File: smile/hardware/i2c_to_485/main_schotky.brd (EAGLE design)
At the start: 34.3 x 45.2 mm, 12 parts, among them IC1 MAX481CSA, IC2 MAX481CSA, U1 7402D

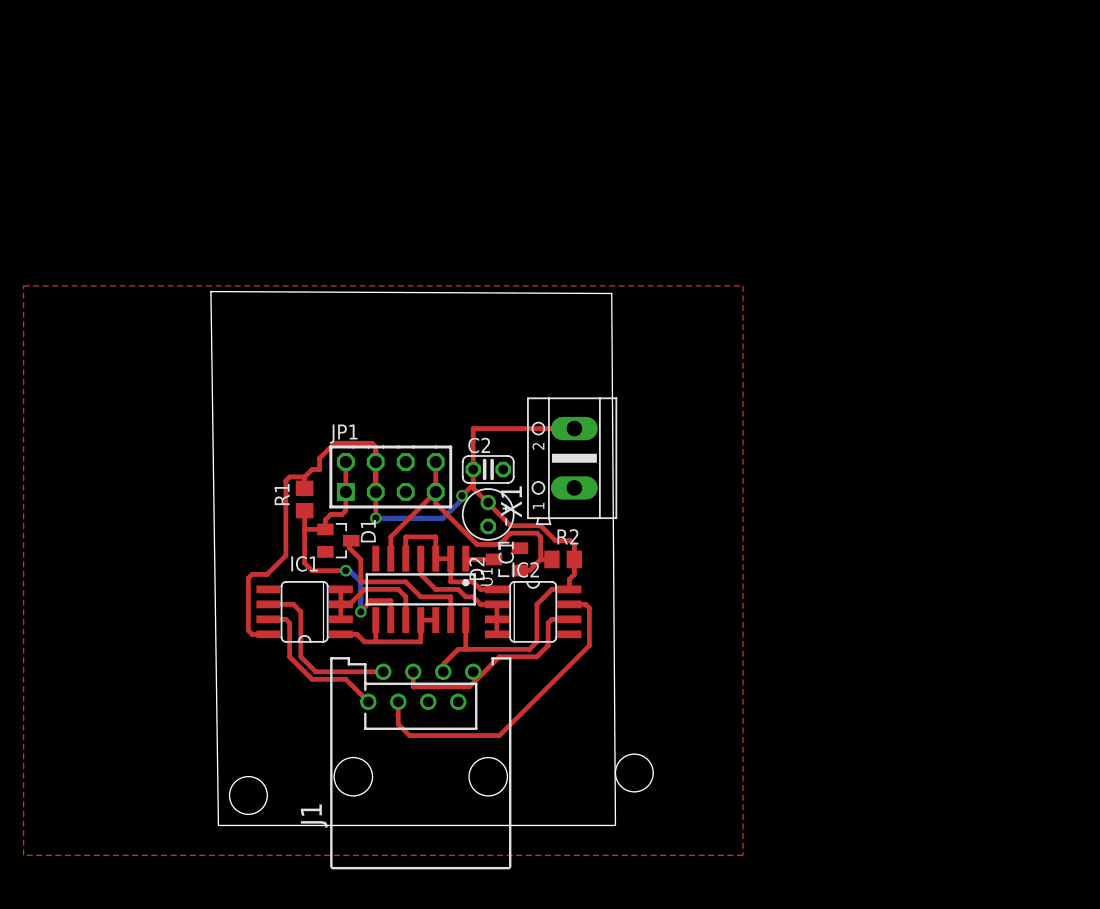
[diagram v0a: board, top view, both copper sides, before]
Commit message: i2c to RS485 updated
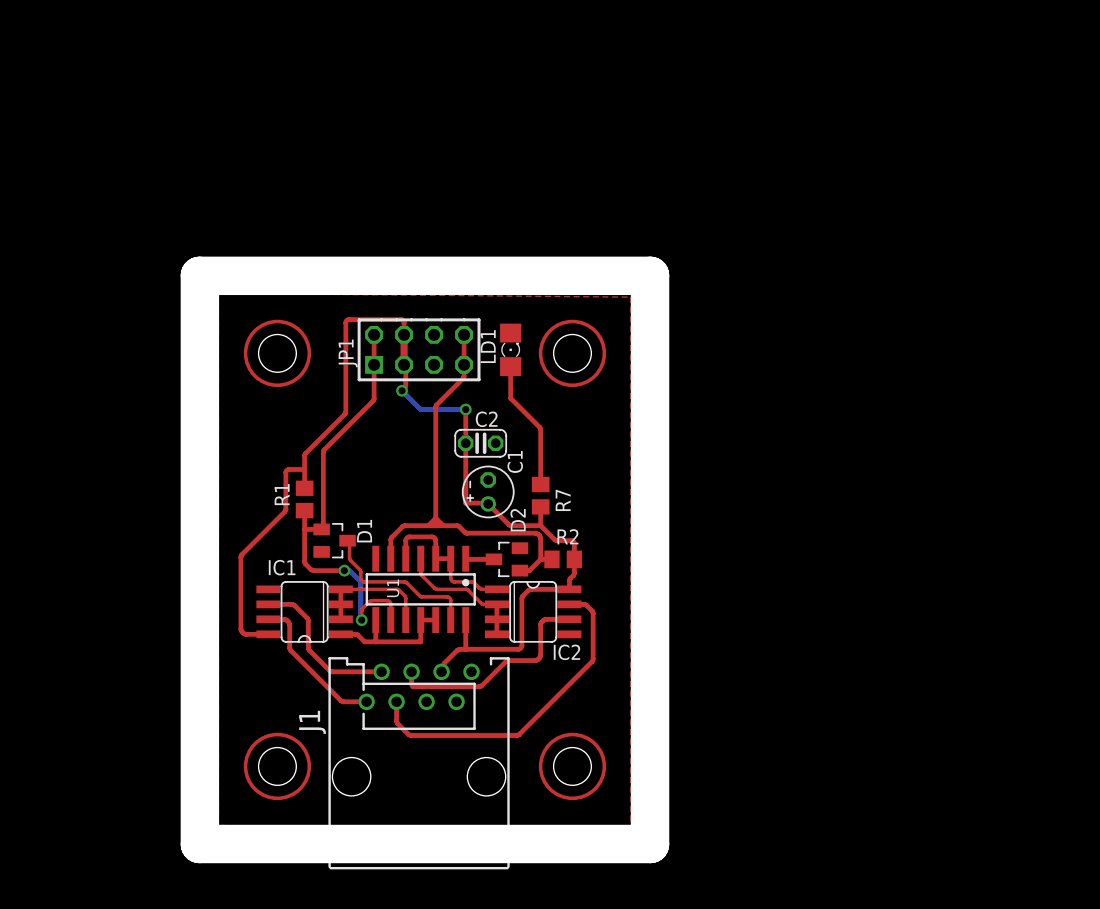
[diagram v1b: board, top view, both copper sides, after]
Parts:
- removed X1: (no value), con-ptr500:AK500/2
- added LD1: (no value), led:1206
- added R7: 4k7, resistor:R0805
- moved JP1 11.0 mm to (17.0, 40.3)
- moved C2 2.31 mm to (22.2, 32.4)
- moved C1 1.91 mm to (22.9, 28.3), turned to 90 degrees
- moved D1 0.32 mm to (9.84, 24.1)
- moved J1 0.14 mm to (17.0, 4.13)
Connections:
- new net N$5: LD1.A, R7.1
- net GND: now also LD1.C; no longer X1.1
- net VCC: now also R7.2; no longer X1.2
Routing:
- net SCL: track 25.8 -> 38.5 mm
- net SDA: track 26.6 -> 39.1 mm
- net N$5: track 0.00 -> 11.2 mm
- net VCC: track 93.1 -> 95.8 mm
- net SDA_B: track 26.6 -> 27.8 mm
- net SCL_A: track 14.3 -> 13.4 mm
- net N$2: track 13.6 -> 13.0 mm
- net SCL_B: track 13.0 -> 12.4 mm
- net N$6: track 11.4 -> 10.8 mm
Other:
- board size 34.3 x 45.2 mm -> 38.2 x 48.2 mm

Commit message: i2c to rs485 - testing version
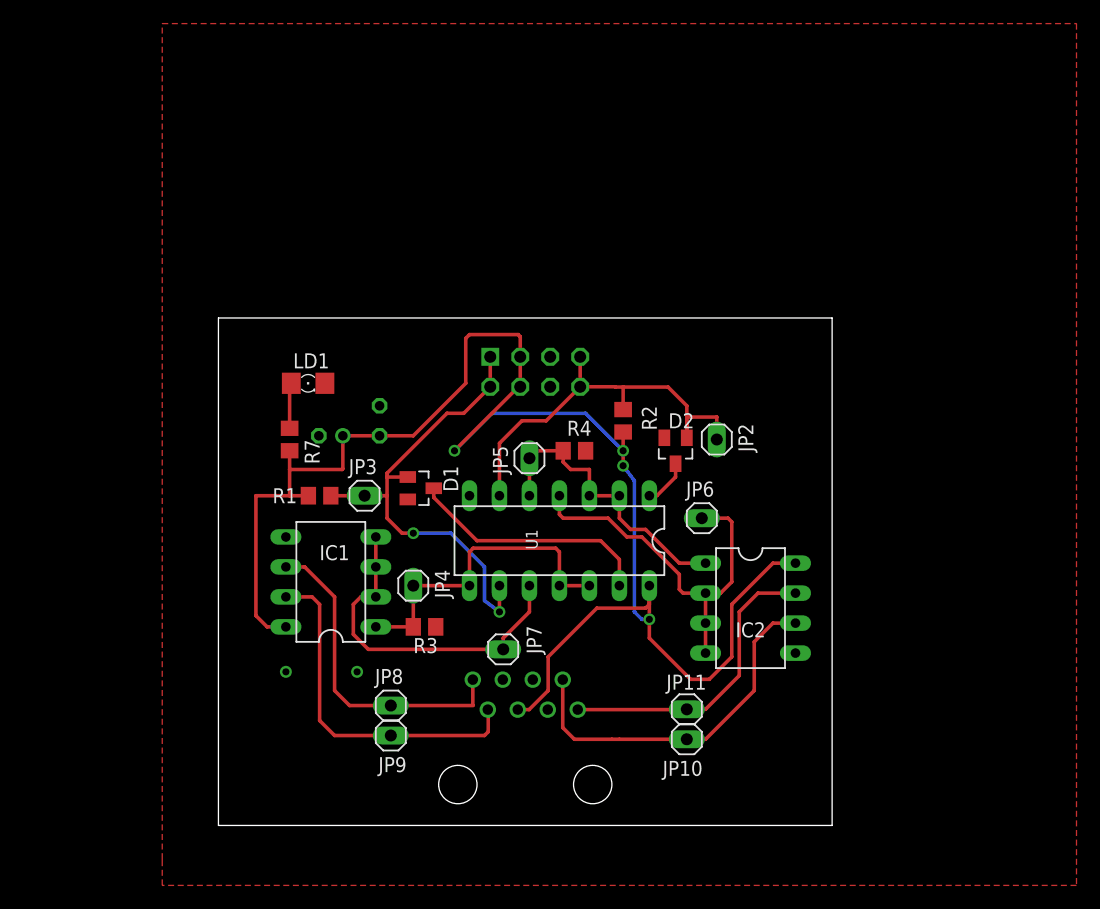
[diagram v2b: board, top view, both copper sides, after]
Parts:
- added JP10, JP11, JP2, JP3, JP4, JP5, JP6, JP7, JP8, JP9: (no value), pinhead_v2:1X01
- added R3, R4: 10k, resistor:R0805
- IC1, IC2: value MAX481CSA -> MAX485DIL; device maxim:SO08 -> maxim:DIL08
- U1: value 7402D -> 7402N; device 74xx-us:SO14 -> 74xx-us:DIL14
- moved R7 21.8 mm to (6.03, 32.7)
- moved IC2 18.4 mm to (45.1, 18.4)
- moved LD1 17.4 mm to (7.60, 37.5), turned to 0 degrees
- moved D2 17.0 mm to (38.7, 31.8), turned to 180 degrees
- moved C1 14.2 mm to (9.53, 33.0), flipped to the bottom, turned to 0 degrees
- moved R2 12.8 mm to (34.3, 34.3), turned to 270 degrees
- moved U1 12.5 mm to (28.9, 24.1)
- moved JP1 10.0 mm to (26.8, 38.4), flipped to the bottom, turned to 180 degrees
- moved J1 9.02 mm to (26.0, 3.46), flipped to the bottom
- moved C2 8.78 mm to (13.7, 34.3), flipped to the bottom, turned to 90 degrees
- moved D1 8.55 mm to (17.1, 28.6)
- moved IC1 3.38 mm to (9.53, 20.6)
- moved R1 1.31 mm to (8.57, 27.9), turned to 180 degrees
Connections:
- net GND: now also J1.4, R3.2, R4.2; no longer J1.5
- net N$1: now also JP6.1
- net N$2: now also JP5.1, R4.1
- net N$6: now also JP7.1
- net N$7: now also JP4.1, R3.1
- net SCL: now also JP3.1
- net SCL_A: now also J1.8, JP8.1; no longer J1.2
- net SCL_B: now also J1.7, JP9.1; no longer J1.1
- net SDA: now also JP2.1
- net SDA_A: now also J1.2, JP10.1; no longer J1.4
- net SDA_B: now also J1.1, JP11.1; no longer J1.3
- net VCC: now also J1.5; no longer J1.6
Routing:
- net VCC: track 95.8 -> 138.8 mm, vias 2 -> 4
- net N$1: track 11.3 -> 32.9 mm
- net N$6: track 10.8 -> 29.3 mm
- net SCL_B: track 12.4 -> 29.8 mm
- net N$7: track 12.0 -> 29.2 mm
- net SCL_A: track 13.4 -> 27.6 mm
- net N$2: track 13.0 -> 25.4 mm
- net SDA_A: track 18.5 -> 30.7 mm
- net N$5: track 11.2 -> 3.87 mm
- net N$3: track 13.7 -> 20.9 mm
- net SDA: track 39.1 -> 35.2 mm
- net SCL: track 38.5 -> 41.3 mm
- net SDA_B: track 27.8 -> 25.7 mm
- net N$4: track 2.42 -> 4.00 mm
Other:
- board size 38.2 x 48.2 mm -> 52 x 43 mm
